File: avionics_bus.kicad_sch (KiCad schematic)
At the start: 10 parts

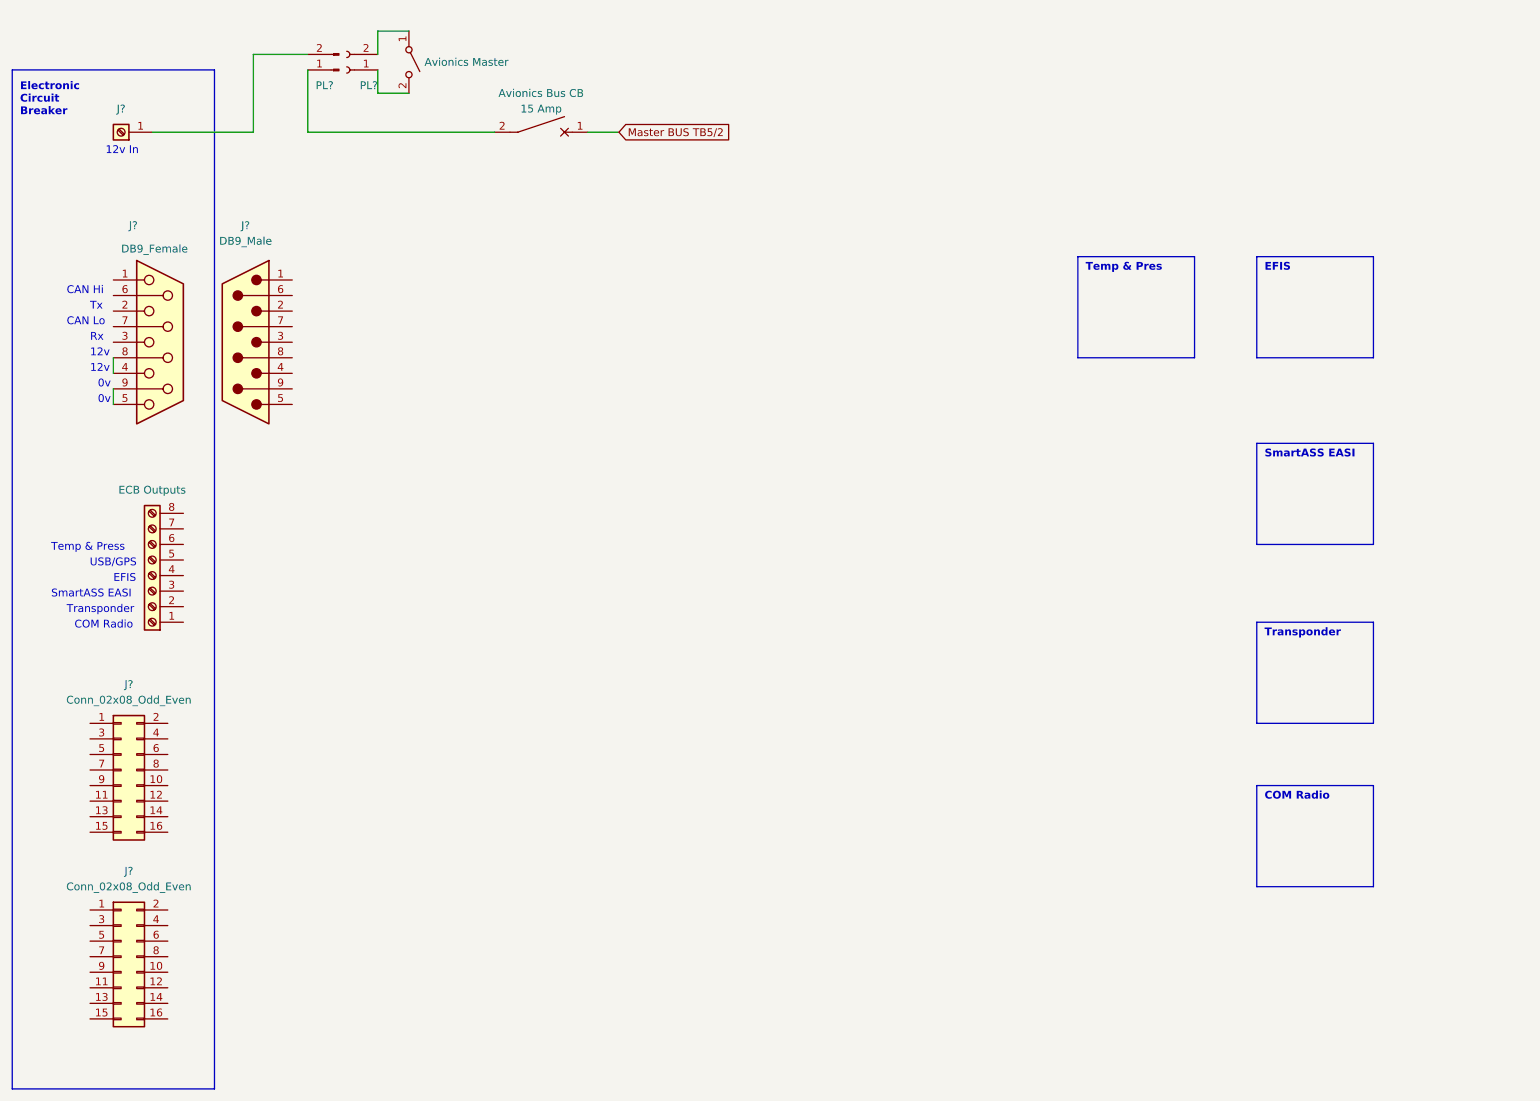
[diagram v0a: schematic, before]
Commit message: Upated Avionics Bus
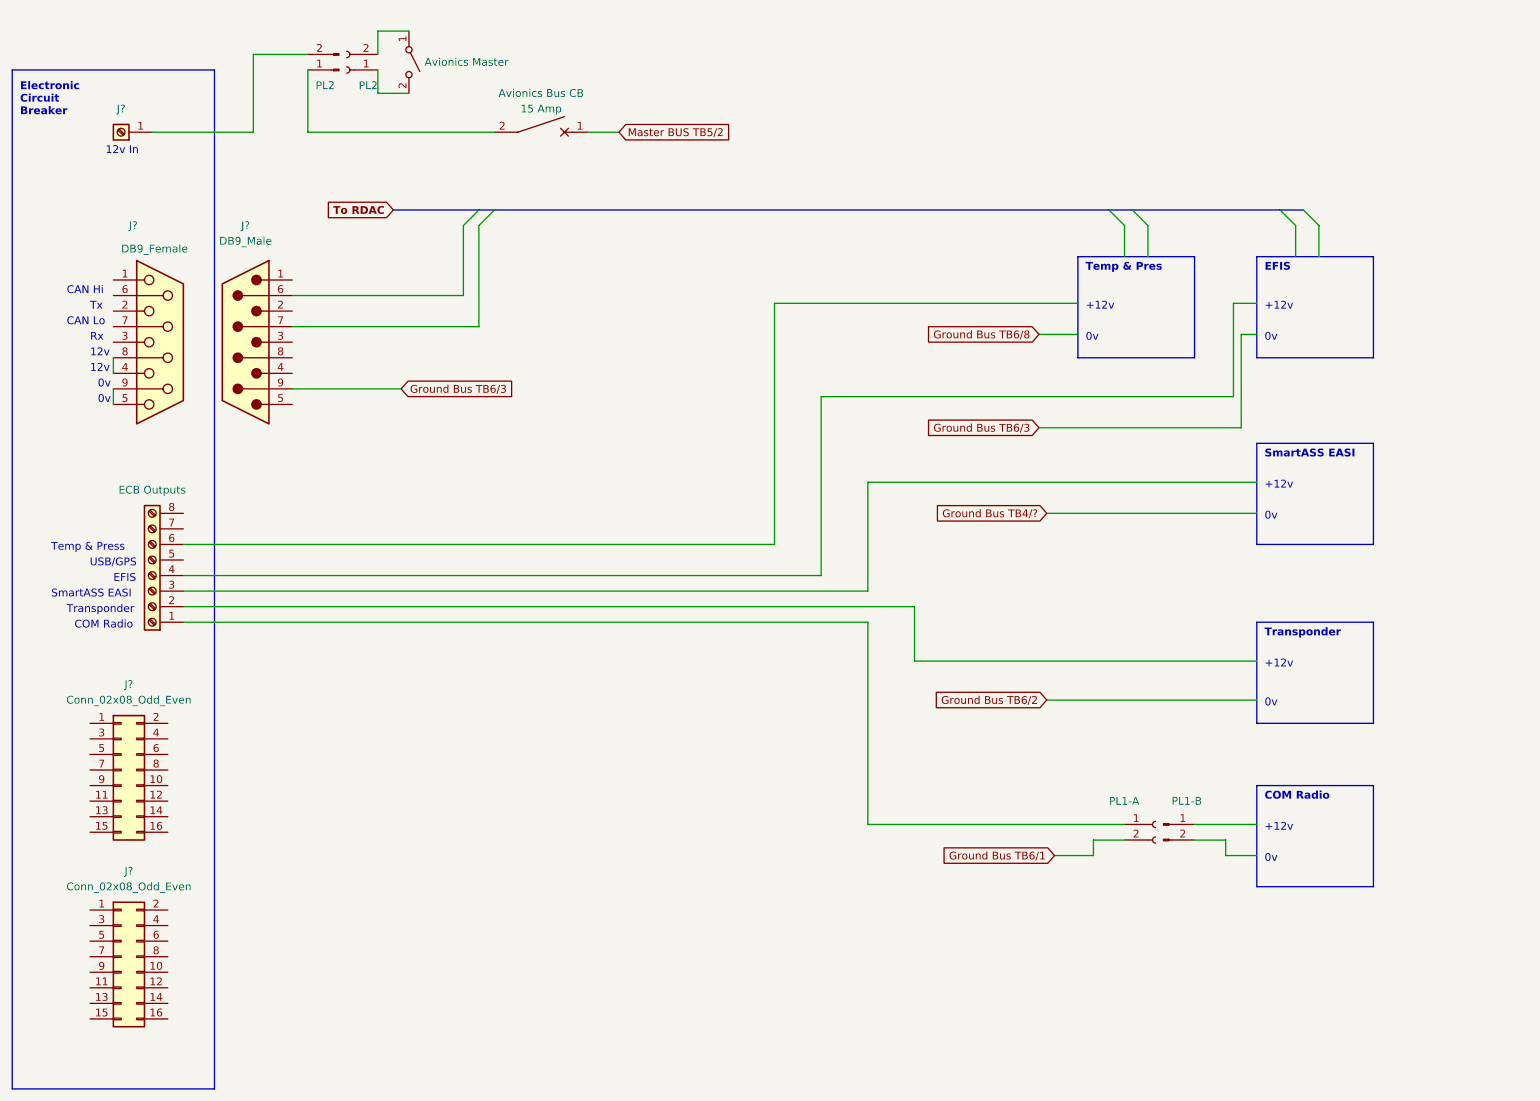
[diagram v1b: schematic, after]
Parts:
- added PL1-A: Conn_01x02_Female, symbol Connector:Conn_01x02_Female
- added PL1-B: Conn_01x02_Male, symbol Connector:Conn_01x02_Male
- gave numbers to parts that had none: 1
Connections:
- net at J?.1 (Pin_1): now also PL1-A.1 (Pin_1)
- net Ground Bus TB6/3: now reaches J?.9
- new net Ground Bus TB6/1: PL1-A.2 (Pin_2)
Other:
- note added: "+12v"
- title: (none) -> Europa Avionics Bus

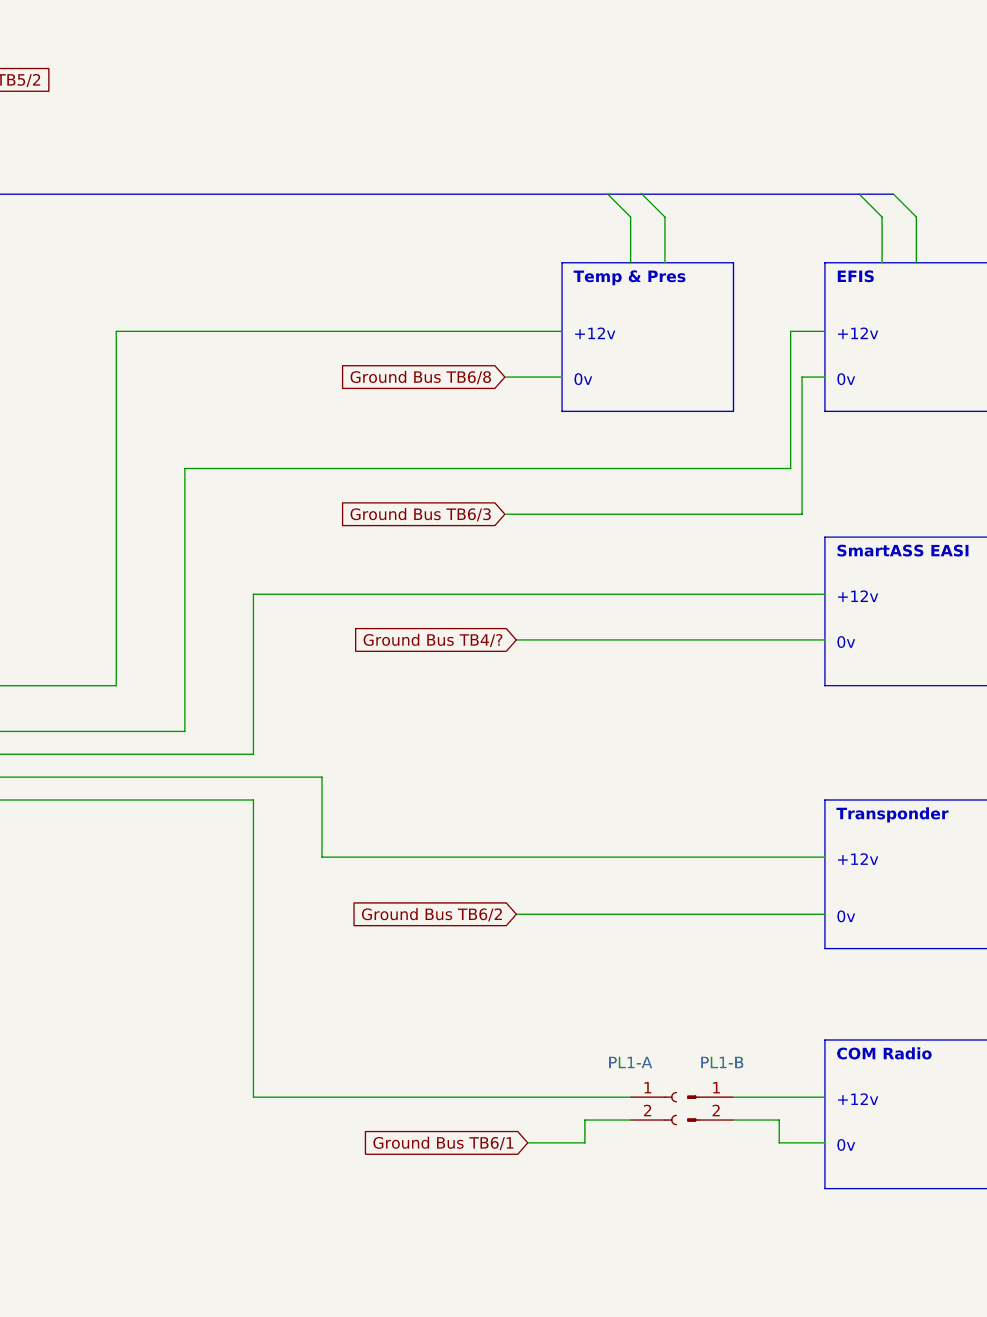
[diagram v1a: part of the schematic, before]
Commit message: Small updates to Avionics Bus
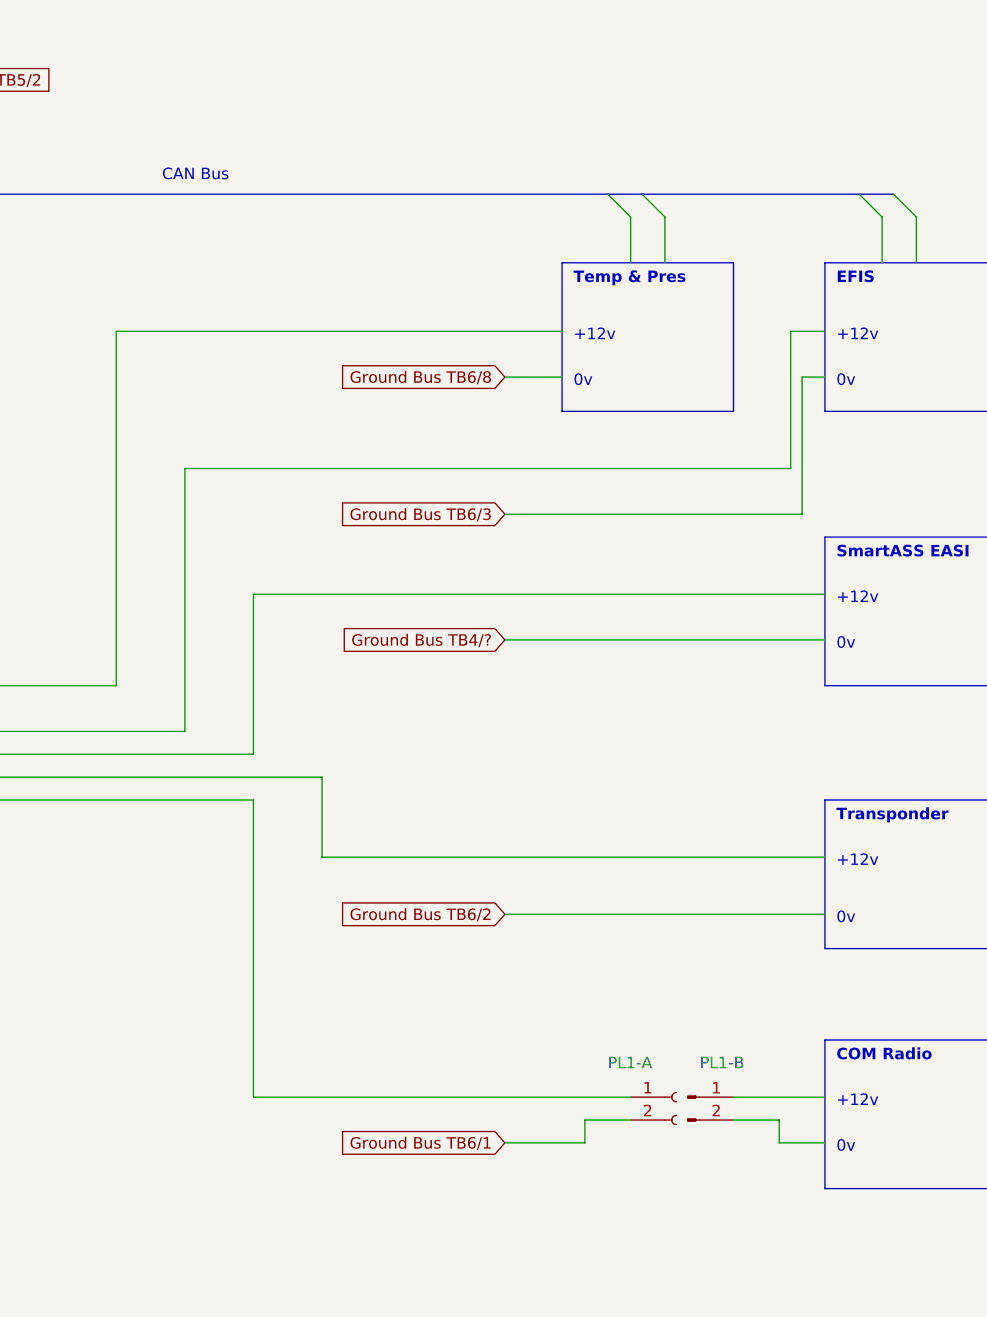
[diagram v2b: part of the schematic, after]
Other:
- note added: "CAN Bus"
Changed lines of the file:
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@@
+    (stroke (width 0) (type default) (color 0 0 0 0))
+  )
+  (bus_entry (at 212.09 46.99) (size 2.54 2.54)
+    (stroke (width 0) (type default) (color 0 0 0 0))
+  )
+  (bus_entry (at 215.9 46.99) (size 2.54 2.54)
     (stroke (width 0) (type default) (color 0 0 0 0))
   )
@@
     (stroke (width 0) (type default) (color 0 0 0 0))
   )
-  (bus_entry (at 212.09 46.99) (size 2.54 2.54)
-    (stroke (width 0) (type default) (color 0 0 0 0))
-  )
-  (bus_entry (at 215.9 46.99) (size 2.54 2.54)
-    (stroke (width 0) (type default) (color 0 0 0 0))
-  )
   (wire (pts (xy 60.96 111.76) (xy 180.34 111.76))
     (stroke (width 0) (type default) (color 0 0 0 0))
@@
     (stroke (width 0) (type default) (color 0 0 0 0))
   )
-  (wire (pts (xy 201.93 96.52) (xy 236.22 96.52))
+  (wire (pts (xy 200.66 96.52) (xy 236.22 96.52))
     (stroke (width 0) (type default) (color 0 0 0 0))
   )
@@
     (stroke (width 0) (type default) (color 0 0 0 0))
   )
-  (wire (pts (xy 209.55 152.4) (xy 203.2 152.4))
+  (wire (pts (xy 209.55 152.4) (xy 200.66 152.4))
     (stroke (width 0) (type default) (color 0 0 0 0))
   )
@@
     (stroke (width 0) (type default) (color 0 0 0 0))
   )
-  (wire (pts (xy 201.93 127) (xy 236.22 127))
+  (wire (pts (xy 200.66 127) (xy 236.22 127))
     (stroke (width 0) (type default) (color 0 0 0 0))
   )
@@
     (effects (font (size 1.27 1.27)) (justify left bottom))
   )
+  (text "CAN Bus" (at 162.56 45.72 0)
+    (effects (font (size 1.27 1.27)) (justify left bottom))
+  )
   (text "Transponder" (at 237.49 116.84 0)
     (effects (font (size 1.27 1.27) bold) (justify left bottom))
@@
     (effects (font (size 1.27 1.27)) (justify left bottom))
   )
-  (global_label "Ground Bus TB4{slash}?" (shape input) (at 201.93 96.52 180) (fields_autoplaced)
+  (global_label "Ground Bus TB4{slash}?" (shape input) (at 200.66 96.52 180) (fields_autoplaced)
     (effects (font (size 1.27 1.27)) (justify right))
-    (property "Intersheet References" "${INTERSHEET_REFS}" (id 0) (at 181.6159 96.4406 0)
+    (property "Intersheet References" "${INTERSHEET_REFS}" (id 0) (at 180.3459 96.4406 0)
       (effects (font (size 1.27 1.27)) (justify right) hide)
     )
@@
     )
   )
-  (global_label "Ground Bus TB6{slash}1" (shape input) (at 203.2 152.4 180) (fields_autoplaced)
+  (global_label "Ground Bus TB6{slash}1" (shape input) (at 200.66 152.4 180) (fields_autoplaced)
     (effects (font (size 1.27 1.27)) (justify right))
-    (property "Intersheet References" "${INTERSHEET_REFS}" (id 0) (at 182.765 152.3206 0)
+    (property "Intersheet References" "${INTERSHEET_REFS}" (id 0) (at 180.225 152.3206 0)
       (effects (font (size 1.27 1.27)) (justify right) hide)
     )
   )
-  (global_label "Ground Bus TB6{slash}2" (shape input) (at 201.93 127 180) (fields_autoplaced)
+  (global_label "Ground Bus TB6{slash}2" (shape input) (at 200.66 127 180) (fields_autoplaced)
     (effects (font (size 1.27 1.27)) (justify right))
-    (property "Intersheet References" "${INTERSHEET_REFS}" (id 0) (at 181.495 126.9206 0)
+    (property "Intersheet References" "${INTERSHEET_REFS}" (id 0) (at 180.225 126.9206 0)
       (effects (font (size 1.27 1.27)) (justify right) hide)
     )

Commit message: Proof reading and snagging updates
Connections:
- net Ground Bus TB6/3: no longer J?.9
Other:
- note added: "PL11"
- note added: "PL16"
- note added: "PL7"
- note added: "PL8"
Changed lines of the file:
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@@
-    (stroke (width 0) (type default) (color 0 0 0 0))
-  )
-  (wire (pts (xy 78.74 76.2) (xy 96.52 76.2))
     (stroke (width 0) (type default) (color 0 0 0 0))
   )
@@
     (effects (font (size 1.27 1.27)) (justify left bottom))
   )
+  (text "PL16" (at 229.87 124.46 0)
+    (effects (font (size 1.27 1.27)) (justify left bottom))
+  )
   (text "+12v" (at 237.49 121.92 0)
+    (effects (font (size 1.27 1.27)) (justify left bottom))
+  )
+  (text "PL11" (at 229.87 93.98 0)
     (effects (font (size 1.27 1.27)) (justify left bottom))
   )
@@
     (effects (font (size 1.27 1.27)) (justify left bottom))
   )
+  (text "PL8" (at 231.14 60.96 0)
+    (effects (font (size 1.27 1.27)) (justify left bottom))
+  )
   (text "Transponder" (at 237.49 116.84 0)
     (effects (font (size 1.27 1.27) bold) (justify left bottom))
+  )
+  (text "PL7" (at 201.93 64.77 0)
+    (effects (font (size 1.27 1.27)) (justify left bottom))
   )
   (text "+12v" (at 237.49 92.71 0)
@@
     (effects (font (size 1.27 1.27)) (justify left bottom))
   )
-  (global_label "Ground Bus TB4{slash}?" (shape input) (at 200.66 96.52 180) (fields_autoplaced)
+  (global_label "Ground Bus TB4{slash}6" (shape input) (at 200.66 96.52 180) (fields_autoplaced)
     (effects (font (size 1.27 1.27)) (justify right))
-    (property "Intersheet References" "${INTERSHEET_REFS}" (id 0) (at 180.3459 96.4406 0)
+    (property "Intersheet References" "${INTERSHEET_REFS}" (id 0) (at 180.225 96.4406 0)
       (effects (font (size 1.27 1.27)) (justify right) hide)
     )
@@
     )
   )
-  (global_label "Ground Bus TB6{slash}3" (shape input) (at 96.52 76.2 0) (fields_autoplaced)
-    (effects (font (size 1.27 1.27)) (justify left))
-    (property "Intersheet References" "${INTERSHEET_REFS}" (id 0) (at 116.955 76.1206 0)
-      (effects (font (size 1.27 1.27)) (justify left) hide)
-    )
-  )
